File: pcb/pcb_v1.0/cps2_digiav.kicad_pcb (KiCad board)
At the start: 2 copper layers, 103.4 x 48.7 mm, 127 parts, among them J1 Conn_02x05, J2 Conn_02x05, J4 HDMI_CONN, P1 JTAG_CONN, U1 ADV7513, U10 S25FL116K, U12 TLV70012, U13 TLV70025, U14 TLV70012, U15 TLV70018, U16 TLV70018, U2 EP4CE15E22, U3 IT6613, U31 74LVC245, U32 74LVC245, U33 74LVC245, U34 SN74LVC3G17, U7 TC1262-3.3VDBTR, U8 TLV70033

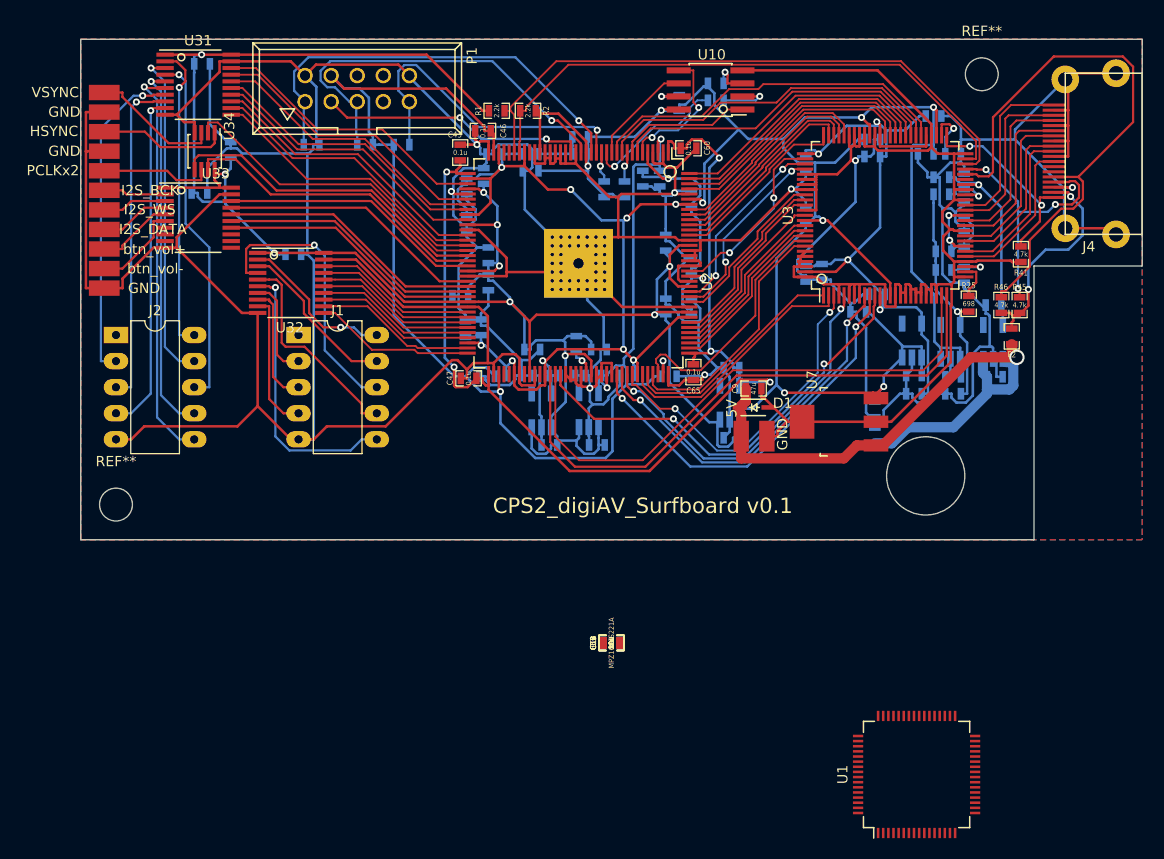
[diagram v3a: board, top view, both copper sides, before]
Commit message: initial layout of ADV7513
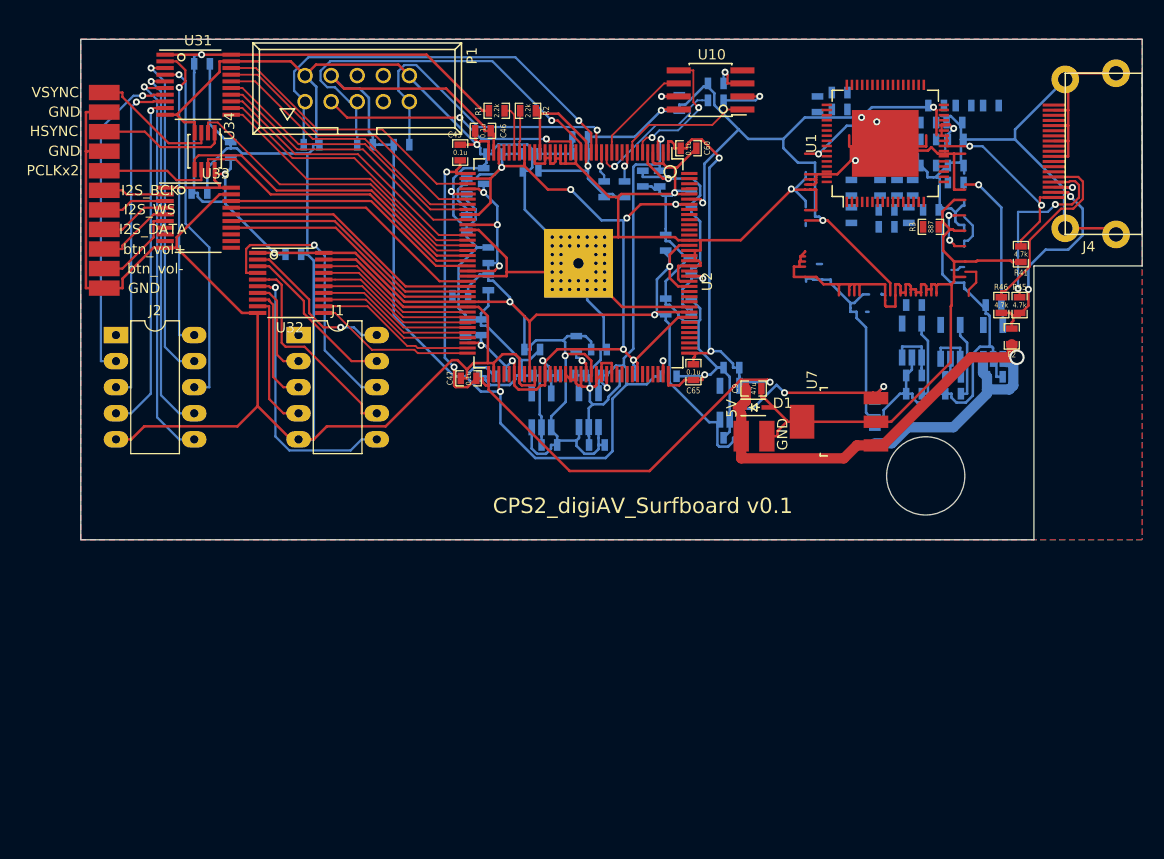
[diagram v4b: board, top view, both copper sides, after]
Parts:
- removed R25: 698, custom_components:SM0603_Resistor_libcms
- removed R26: 1k, custom_components:SM0603_Resistor_libcms
- removed REF** (x2): MountingHole_3.2mm_M3, Mounting_Holes:MountingHole_3.2mm_M3
- removed U3: IT6613, custom_components:TQFP-100_custom
- C10, C11, C12, C13, FB3: moved to B.Cu
- U1: footprint Housings_QFP:LQFP-64_10x10mm_Pitch0.5mm -> Housings_QFP:LQFP-64-1EP_10x10mm_Pitch0.5mm
- moved U1 61.5 mm to (117.5, 33.7)
- moved C11 60.7 mm to (124.2, 31.6)
- moved C13 59.4 mm to (124.3, 33.3)
- moved FB3 56.5 mm to (113.0, 30.4), turned to 180 degrees
- moved C12 51.5 mm to (117.0, 38.0), turned to 90 degrees
- moved R3 51.1 mm to (121.9, 41.8)
- moved C10 47.8 mm to (114.2, 40.6), turned to 270 degrees
- moved C75 24.3 mm to (127.8, 30.0), turned to 0 degrees
- moved C74 21.5 mm to (113.0, 28.7), turned to 180 degrees
- moved C77 19.4 mm to (110.9, 29.8)
- moved C79 14.0 mm to (121.7, 33.3), turned to 180 degrees
- moved C73 13.2 mm to (120.1, 38.0), turned to 90 degrees
- moved C82 12.6 mm to (121.7, 31.6), turned to 180 degrees
- moved C69 10.6 mm to (118.6, 38.0), turned to 90 degrees
- moved C78 10.5 mm to (122.4, 30.0), turned to 180 degrees
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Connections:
- J1 pad 1: Net-(J1-Pad1) -> (no net)
- J2 pad 1: Net-(J2-Pad1) -> (no net)
- J4 pad 13: Net-(J4-Pad13) -> (no net)
- J4 pad 14: Net-(J4-Pad14) -> (no net)
- P1 pad 6: Net-(P1-Pad6) -> (no net)
- P1 pad 7: Net-(P1-Pad7) -> (no net)
- P1 pad 8: Net-(P1-Pad8) -> (no net)
- U1 pad 3: Net-(U1-Pad3) -> (no net)
- U1 pad 30: Net-(U1-Pad30) -> (no net)
- U1 pad 32: Net-(U1-Pad32) -> (no net)
- U1 pad 6: Net-(U1-Pad6) -> (no net)
- U1 pad 7: Net-(U1-Pad7) -> (no net)
- U1 pad 8: Net-(U1-Pad8) -> (no net)
- U2 pad 28: Net-(U2-Pad28) -> (no net)
- U2 pad 32: Net-(U2-Pad32) -> (no net)
- U2 pad 33: Net-(U2-Pad33) -> (no net)
- U2 pad 76: Net-(U2-Pad76) -> (no net)
- U2 pad 77: Net-(U2-Pad77) -> (no net)
- U2 pad 80: Net-(U2-Pad80) -> (no net)
- U2 pad 83: Net-(U2-Pad83) -> (no net)
- U33 pad 11: Net-(U33-Pad11) -> (no net)
- U33 pad 12: Net-(U33-Pad12) -> (no net)
- U33 pad 13: Net-(U33-Pad13) -> (no net)
- U33 pad 7: Net-(U33-Pad7) -> (no net)
- U33 pad 8: Net-(U33-Pad8) -> (no net)
- U33 pad 9: Net-(U33-Pad9) -> (no net)
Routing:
- net /fpga1/SCL: track 58.4 -> 4.78 mm
- net /fpga1/HDMITX_INT_N: track 49.0 -> 1.84 mm
- net /fpga1/HDMITX_I2S_BCK: track 40.4 -> 0.00 mm, vias 2 -> 0
- net /hdmitx1/PVDD1V8: track 46.7 -> 7.59 mm, vias 3 -> 0
- net /fpga1/SDA: track 43.1 -> 4.09 mm
- net /fpga1/HDMITX_I2S_WS: track 37.4 -> 0.00 mm, vias 2 -> 0
- net /hdmitx1/DDCSCL: track 53.3 -> 18.5 mm
- net /fpga1/HDMITX_R7: track 34.8 -> 0.00 mm
- net /fpga1/HDMITX_I2S_DATA: track 34.1 -> 0.00 mm, vias 1 -> 0
- net /fpga1/HDMITX_R6: track 33.4 -> 0.00 mm
- net /fpga1/AUD_MCLK: track 32.4 -> 0.00 mm, vias 1 -> 0
- net /fpga1/HDMITX_R5: track 31.2 -> 0.00 mm
- net /fpga1/HDMITX_RESET_N: track 29.4 -> 0.00 mm
- net Net-(U3-Pad25): track 27.1 -> 0.00 mm
- net /fpga1/HDMITX_R4: track 25.3 -> 0.00 mm
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
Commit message: Reordered inputs, improved clock layout
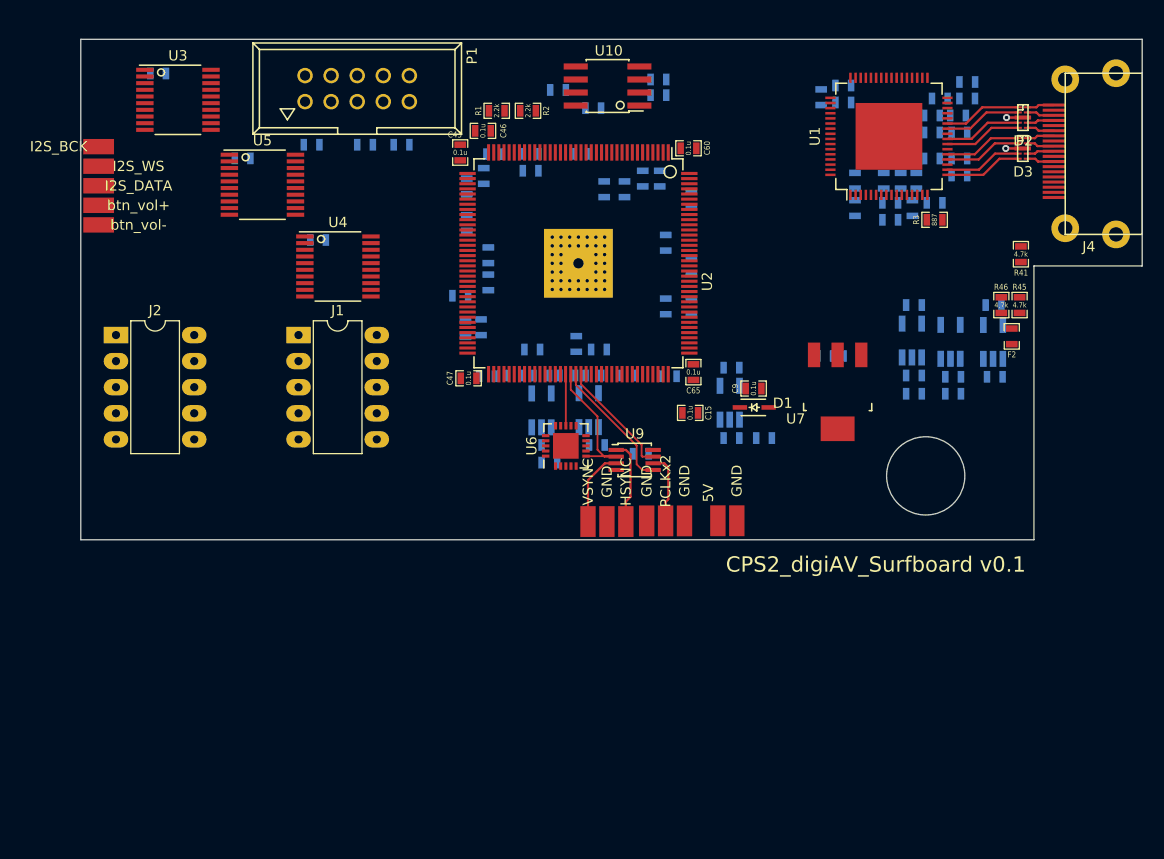
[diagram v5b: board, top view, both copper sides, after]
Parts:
- removed U31, U32, U33: 74LVC245, custom_components:TSSOP-20_4.4x6.5mm_Pitch0.65mm_Handsoldering
- removed U34: SN74LVC3G17, custom_components:SSOP-8_3x3mm_Pitch0.65mm
- removed W19: btn_vol+, custom_components:SMD_PAD
- removed W20: I2S_BCK, custom_components:SMD_PAD
- removed W21: PCLKx2, custom_components:SMD_PAD
- removed W22: I2S_WS, custom_components:SMD_PAD
- removed W23: btn_vol-, custom_components:SMD_PAD
- removed W24: VSYNC, custom_components:SMD_PAD
- removed W25: I2S_DATA, custom_components:SMD_PAD
- removed W26: HSYNC, custom_components:SMD_PAD
- removed W29, W30, W31: GND, custom_components:SMD_PAD
- added C14: 0.1u, custom_components:SM0603_Capa_libcms, B.Cu at (93.7, 63.9)
- added C15: 0.1u, custom_components:SM0603_Capa_libcms, F.Cu at (98.5, 59.9)
- added D2: RClamp0524P, Custom_OSSC:SLP2510P8, F.Cu at (130.9, 31.1)
- added D3: RClamp0524P, Custom_OSSC:SLP2510P8, F.Cu at (130.9, 34.2)
- added R4: 4.7k, custom_components:SM0603_Resistor_libcms, B.Cu at (84.8, 64.7)
- added U3: 74LVC245, custom_components:TSSOP-20_4.4x6.5mm_Pitch0.65mm_Handsoldering, F.Cu at (48.6, 29.4)
- added U4: 74LVC245, custom_components:TSSOP-20_4.4x6.5mm_Pitch0.65mm_Handsoldering, F.Cu at (64.2, 45.6)
- added U5: 74LVC245, custom_components:TSSOP-20_4.4x6.5mm_Pitch0.65mm_Handsoldering, F.Cu at (56.8, 37.7)
- added U6: SI5351C-B, Housings_DFN_QFN:QFN-20-1EP_4x4mm_Pitch0.5mm, F.Cu at (86.4, 63.1)
- added U9: SN74LVC3G17, custom_components:SSOP-8_3x3mm_Pitch0.65mm, F.Cu at (93.1, 64.5)
- added W10: GND, custom_components:SMD_PAD, F.Cu at (94.2, 70.4)
- added W11: HSYNC, custom_components:SMD_PAD, F.Cu at (92.2, 70.5)
- added W12: VSYNC, custom_components:SMD_PAD, F.Cu at (88.5, 70.5)
- added W13: PCLKx2, custom_components:SMD_PAD, F.Cu at (96.1, 70.4)
- added W3: I2S_WS, custom_components:SMD_PAD, F.Cu at (40.9, 35.9)
- added W4: I2S_DATA, custom_components:SMD_PAD, F.Cu at (40.9, 37.8)
- added W5: btn_vol+, custom_components:SMD_PAD, F.Cu at (40.9, 39.7)
- added W6: btn_vol-, custom_components:SMD_PAD, F.Cu at (40.9, 41.6)
- added W7: GND, custom_components:SMD_PAD, F.Cu at (90.4, 70.5)
- added W8: GND, custom_components:SMD_PAD, F.Cu at (97.9, 70.4)
- added W9: GND, custom_components:SMD_PAD, F.Cu at (103.0, 70.4)
- C5: value 0.1u -> 47u
- C9: value 47u -> 0.1u
- W2: value GND -> I2S_BCK
- moved C5 65.8 mm to (105.7, 62.4), turned to 0 degrees
- moved C6 22.0 mm to (46.6, 26.8)
- moved C7 12.4 mm to (62.2, 43.1)
- moved R19 11.9 mm to (85.6, 28.4), turned to 180 degrees
- moved U10 10.0 mm to (90.4, 28.1)
- moved W1 8.55 mm to (101.2, 70.4)
- moved C1 8.07 mm to (114.2, 54.4), turned to 180 degrees
- moved C3 7.10 mm to (111.6, 54.4), turned to 0 degrees
- moved R23 5.61 mm to (95.4, 29.0), turned to 180 degrees
- moved R24 5.60 mm to (95.4, 27.4), turned to 0 degrees
- moved C75 3.25 mm to (125.5, 27.7), turned to 180 degrees
- moved C55 3.07 mm to (89.0, 30.2), turned to 180 degrees
- moved U7 2.92 mm to (112.8, 57.9), turned to 180 degrees
- moved C8 1.42 mm to (54.9, 35.1), turned to 180 degrees
- moved C69 0.77 mm to (119.0, 37.3)
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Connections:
- C101 pad 1: /IOVDD -> /hdmitx1/DVDD3V3
- C108 pad 1: /IOVDD -> /hdmitx1/DVDD3V3
- C3 pad 1: /IOVDD -> /hdmitx1/DVDD3V3
- C4 pad 1: /A33VDD -> /hdmitx1/AVDD3V3
- C40 pad 1: /IOVDD -> /hdmitx1/DVDD3V3
- C45 pad 1: /IOVDD -> /hdmitx1/DVDD3V3
- C5 pad 1: GND -> /input1/5V
- C5 pad 2: /IOVDD -> GND
- C52 pad 1: /IOVDD -> /hdmitx1/DVDD3V3
- C53 pad 1: /IOVDD -> /hdmitx1/DVDD3V3
- C55 pad 2: /IOVDD -> /hdmitx1/DVDD3V3
- C57 pad 1: /IOVDD -> /hdmitx1/DVDD3V3
- C6 pad 2: /IOVDD -> /hdmitx1/DVDD3V3
- C62 pad 1: /IOVDD -> /hdmitx1/DVDD3V3
- C63 pad 1: /IOVDD -> /hdmitx1/DVDD3V3
- C7 pad 2: /IOVDD -> /hdmitx1/DVDD3V3
- C74 pad 1: /hdmitx1/AVDD1V8 -> /hdmitx1/DVDD1V8
- C75 pad 1: /IOVDD -> /hdmitx1/DVDD3V3
- C8 pad 1: /IOVDD -> GND
- C8 pad 2: GND -> /hdmitx1/DVDD3V3
- C86 pad 1: /hdmitx1/PVDD1V8 -> /hdmitx1/AVDD1V8
- C87 pad 1: /A33VDD -> /hdmitx1/DVDD3V3
- C88 pad 1: /A33VDD -> /hdmitx1/AVDD3V3
- C89 pad 1: /hdmitx1/AVDD1V8 -> /hdmitx1/DVDD1V8
- C9 pad 1: /5V -> GND
- C9 pad 2: GND -> /hdmitx1/DVDD3V3
- C90 pad 1: /hdmitx1/PVDD1V8 -> /hdmitx1/AVDD1V8
- C91 pad 1: /IOVDD -> /hdmitx1/DVDD3V3
- C92 pad 1: /IOVDD -> /hdmitx1/DVDD3V3
- C94 pad 1: /IOVDD -> /hdmitx1/DVDD3V3
- C99 pad 1: /IOVDD -> /hdmitx1/DVDD3V3
- D1 pad 1: /5V -> /input1/5V
- FB2 pad 2: /hdmitx1/PVDD1V8 -> /hdmitx1/AVDD1V8
- FB3 pad 1: /hdmitx1/AVDD1V8 -> /hdmitx1/DVDD1V8
- FB4 pad 1: /IOVDD -> /hdmitx1/DVDD3V3
- J4 pad 1: /hdmitx1/TX2+ -> Net-(D2-Pad10)
- J4 pad 10: /hdmitx1/TXC+ -> Net-(D3-Pad7)
- J4 pad 12: /hdmitx1/TXC- -> Net-(D3-Pad6)
- J4 pad 3: /hdmitx1/TX2- -> Net-(D2-Pad9)
- J4 pad 4: /hdmitx1/TX1+ -> Net-(D2-Pad7)
- J4 pad 6: /hdmitx1/TX1- -> Net-(D2-Pad6)
- J4 pad 7: /hdmitx1/TX0+ -> Net-(D3-Pad10)
- J4 pad 9: /hdmitx1/TX0- -> Net-(D3-Pad9)
- R1 pad 1: /IOVDD -> /hdmitx1/DVDD3V3
- R16 pad 1: /IOVDD -> /hdmitx1/DVDD3V3
- R17 pad 2: /IOVDD -> /hdmitx1/DVDD3V3
- R18 pad 1: /IOVDD -> /hdmitx1/DVDD3V3
- R19 pad 2: /IOVDD -> /hdmitx1/DVDD3V3
- R2 pad 1: /IOVDD -> /hdmitx1/DVDD3V3
- R24 pad 2: /IOVDD -> /hdmitx1/DVDD3V3
- U10 pad 8: /IOVDD -> /hdmitx1/DVDD3V3
- U12 pad 1: /IOVDD -> /hdmitx1/DVDD3V3
- U12 pad 3: /IOVDD -> /hdmitx1/DVDD3V3
- U13 pad 1: /IOVDD -> /hdmitx1/DVDD3V3
- U13 pad 3: /IOVDD -> /hdmitx1/DVDD3V3
- U14 pad 1: /IOVDD -> /hdmitx1/DVDD3V3
- U14 pad 3: /IOVDD -> /hdmitx1/DVDD3V3
- U15 pad 1: /A33VDD -> /hdmitx1/DVDD3V3
- U15 pad 3: /A33VDD -> /hdmitx1/DVDD3V3
- U15 pad 5: /hdmitx1/AVDD1V8 -> /hdmitx1/DVDD1V8
- U16 pad 1: /A33VDD -> /hdmitx1/AVDD3V3
- U16 pad 3: /A33VDD -> /hdmitx1/AVDD3V3
- U16 pad 5: /hdmitx1/PVDD1V8 -> /hdmitx1/AVDD1V8
- U2 pad 113: /fpga1/HDMITX_PCLK -> /hdmitx1/B5
- U2 pad 114: /hdmitx1/B5 -> /hdmitx1/B6
- U2 pad 115: /hdmitx1/B6 -> /hdmitx1/B7
- U2 pad 117: /IOVDD -> /hdmitx1/DVDD3V3
- U2 pad 119: /hdmitx1/B7 -> /hdmitx1/G0
- U2 pad 120: /hdmitx1/G0 -> /fpga1/HDMITX_PCLK
- U2 pad 122: /IOVDD -> /hdmitx1/DVDD3V3
- U2 pad 130: /IOVDD -> /hdmitx1/DVDD3V3
- U2 pad 139: /IOVDD -> /hdmitx1/DVDD3V3
- U2 pad 17: /IOVDD -> /hdmitx1/DVDD3V3
- U2 pad 26: /IOVDD -> /hdmitx1/DVDD3V3
- U2 pad 39: /fpga1/Rin0 -> /input1/F3_O
- U2 pad 40: /IOVDD -> /hdmitx1/DVDD3V3
- U2 pad 42: /fpga1/Rin1 -> /input1/F2_O
- U2 pad 43: /fpga1/Rin2 -> /input1/F1_O
- U2 pad 44: /fpga1/Rin3 -> /input1/F0_O
- U2 pad 46: /fpga1/Gin0 -> /input1/R3_O
- U2 pad 47: /IOVDD -> /hdmitx1/DVDD3V3
- U2 pad 49: /fpga1/Gin1 -> /input1/R2_O
- U2 pad 50: /fpga1/Gin2 -> /input1/R1_O
- U2 pad 51: /fpga1/Gin3 -> /input1/R0_O
- U2 pad 52: /fpga1/PCLKx2_in -> GND
- U2 pad 53: /fpga1/VSYNC_in -> GND
- U2 pad 54: /fpga1/HSYNC_in -> GND
- U2 pad 56: /IOVDD -> /hdmitx1/DVDD3V3
- U2 pad 60: /fpga1/btn_vol+ -> /input1/VOL+_O
- U2 pad 61: /fpga1/btn_vol- -> /input1/VOL-_O
- U2 pad 62: /IOVDD -> /hdmitx1/DVDD3V3
- U2 pad 64: /fpga1/Bin0 -> /input1/G3_O
- U2 pad 65: /fpga1/Bin1 -> /input1/G2_O
- U2 pad 66: /fpga1/Bin2 -> /input1/G1_O
- U2 pad 67: /fpga1/Bin3 -> /input1/G0_O
- U2 pad 68: /fpga1/Fin0 -> /input1/B3_O
- U2 pad 69: /fpga1/Fin1 -> /input1/B2_O
- U2 pad 71: /fpga1/Fin2 -> /input1/B1_O
- U2 pad 72: /fpga1/Fin3 -> /input1/B0_O
- U2 pad 81: /IOVDD -> /hdmitx1/DVDD3V3
- U2 pad 88: GND -> /fpga1/CLK0
- U2 pad 89: GND -> /input1/PCLKx2
- U2 pad 90: GND -> /input1/VSYNC_O
- U2 pad 91: GND -> /input1/HSYNC_O
- U2 pad 93: /IOVDD -> /hdmitx1/DVDD3V3
- U7 pad 3: /IOVDD -> /hdmitx1/DVDD3V3
- U8 pad 5: /A33VDD -> /hdmitx1/AVDD3V3
- W1 pad 1: /5V -> /input1/5V
- W2 pad 1: GND -> Net-(U5-Pad2)
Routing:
- net GND: track 835.0 -> 0.00 mm, vias 12 -> 0
- net /IOVDD: track 335.8 -> 0.00 mm, vias 16 -> 0
- net /fpga1/VCCA: track 132.2 -> 0.00 mm, vias 4 -> 0
- net /fpga1/VCCINT: track 127.9 -> 0.00 mm, vias 11 -> 0
- net /fpga1/VCCD_PLL: track 103.9 -> 0.00 mm, vias 5 -> 0
- net /5V: track 62.9 -> 0.00 mm, vias 1 -> 0
- net /fpga1/TCK: track 42.1 -> 0.00 mm, vias 1 -> 0
- net /fpga1/TMS: track 39.6 -> 0.00 mm, vias 1 -> 0
- net Net-(J2-Pad6): track 39.3 -> 0.00 mm, vias 1 -> 0
- net Net-(J2-Pad7): track 36.3 -> 0.00 mm, vias 1 -> 0
- net Net-(J2-Pad8): track 34.5 -> 0.00 mm, vias 1 -> 0
- net Net-(J2-Pad4): track 33.2 -> 0.00 mm, vias 1 -> 0
- net Net-(J2-Pad9): track 32.5 -> 0.00 mm, vias 1 -> 0
- net Net-(J2-Pad3): track 32.3 -> 0.00 mm, vias 1 -> 0
- net /fpga1/TDI: track 32.1 -> 0.00 mm, vias 1 -> 0
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- removed copper zone on B.Cu, net GND
- removed copper zone on F.Cu, net GND

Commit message: Final changes before pull req
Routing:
- net (no net): track 3.27 -> 0.03 mm, vias 2 -> 0
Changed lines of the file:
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@@
   (general
     (links 505)
-    (no_connects 440)
+    (no_connects 481)
     (area 39.065999 23.467999 142.550001 72.313001)
     (thickness 1.6)
     (drawings 8)
-    (tracks 88)
+    (tracks 84)
     (zones 0)
     (modules 128)
@@
   (gr_line (start 39.116 23.518) (end 142.5 23.518) (angle 90) (layer Edge.Cuts) (width 0.1))
   (segment (start 86.837 61.131) (end 86.86 61.154) (width 0.22) (layer F.Cu) (net 0))
-  (segment (start 130.8608 34.1503) (end 129.2098 34.1503) (width 0.25) (layer F.Cu) (net 0))
-  (via (at 129.2098 34.1503) (size 0.686) (drill 0.35) (layers F.Cu B.Cu) (net 0))
-  (segment (start 130.8735 31.1404) (end 129.286 31.1404) (width 0.25) (layer F.Cu) (net 0))
-  (via (at 129.286 31.1404) (size 0.686) (drill 0.35) (layers F.Cu B.Cu) (net 0))
   (segment (start 98.483 51.181) (end 98.387 51.085) (width 0.18) (layer F.Cu) (net 33))
   (segment (start 98.451 49.149) (end 98.387 49.085) (width 0.18) (layer F.Cu) (net 35))
